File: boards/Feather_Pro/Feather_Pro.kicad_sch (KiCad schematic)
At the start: 45 parts, among them J101 SMA, J102 USB4105-GF-A, J201 TestPoint, SW101 SW_Push, SW102 SW_Push, SW103 SW_SPST, SW104 SW_Push, SW105 SW_Push, U1 LCD_2.2_in, U101 E22-400MM22S, U103 ECMF02-2AMX6, U104 ESP32-S3-MINI-1U, U107 LR2021, U203 TPS2121

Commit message: Connected button to mcu gpio pins
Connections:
- net BUTTON_DOWN: now also U104.8 (IO4)
- net BUTTON_LEFT: now also U104.5 (IO1)
- net BUTTON_RIGHT: now also U104.6 (IO2)
- net BUTTON_UP: now also U104.9 (IO5); no longer C103.2, SW102.2
- net BUTTON_CENTER: now reaches U104.7 (IO3)
- net BUTTON_CENTER: now also C103.2, SW102.2
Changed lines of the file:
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@@
+		)
+	)
+	(hierarchical_label "BUTTON_DOWN"
+		(shape input)
+		(at 229.87 64.77 180)
+		(effects
+			(font
+				(size 1.27 1.27)
+			)
+			(justify right)
 		)
 	)
@@
 		)
 	)
+	(hierarchical_label "BUTTON_CENTER"
+		(shape input)
+		(at 229.87 62.23 180)
+		(effects
+			(font
+				(size 1.27 1.27)
+			)
+			(justify right)
+		)
+	)
 	(hierarchical_label "USB_D+"
 		(shape bidirectional)
@@
 		)
 	)
-	(hierarchical_label "BUTTON_UP"
+	(hierarchical_label "BUTTON_CENTER"
 		(shape input)
 		(at 223.52 135.89 180)
@@
 		)
 	)
+	(hierarchical_label "BUTTON_RIGHT"
+		(shape input)
+		(at 229.87 59.69 180)
+		(effects
+			(font
+				(size 1.27 1.27)
+			)
+			(justify right)
+		)
+	)
 	(hierarchical_label "USB_POWER"
 		(shape output)
@@
 		(effects
 			(font
+				(size 1.27 1.27)
+			)
+			(justify right)
+		)
+	)
+	(hierarchical_label "BUTTON_UP"
+		(shape input)
+		(at 229.87 67.31 180)
+		(effects
+			(font
+				(size 1.27 1.27)
+			)
+			(justify right)
+		)
+	)
+	(hierarchical_label "BUTTON_LEFT"
+		(shape input)
+		(at 229.87 57.15 180)
+		(effects
+			(font

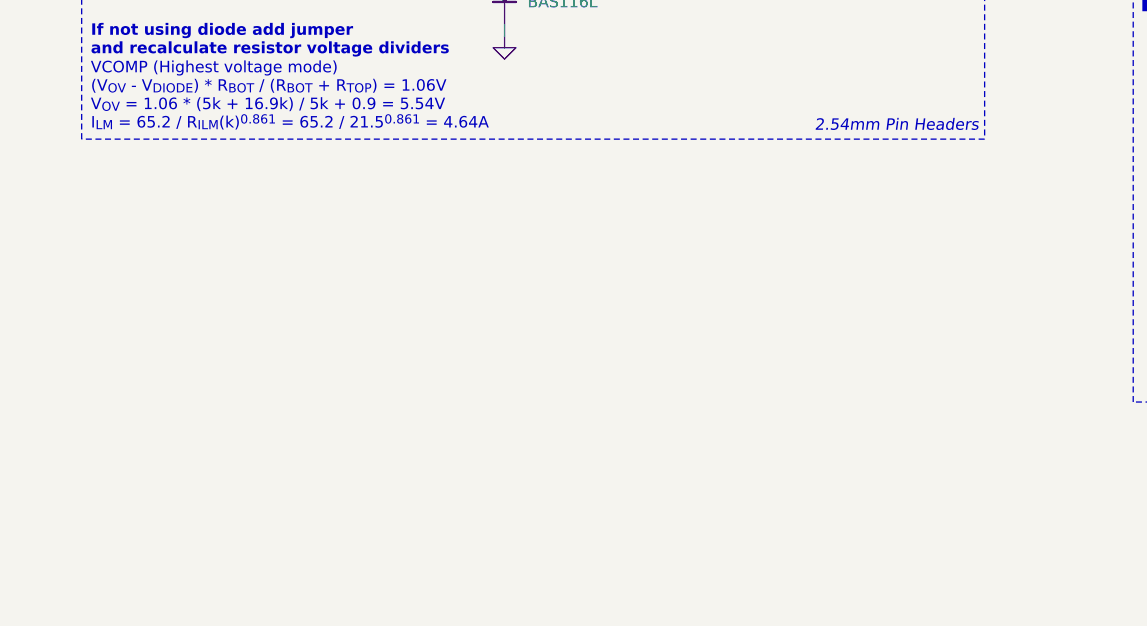
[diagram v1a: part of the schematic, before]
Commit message: Added SD Card Reader
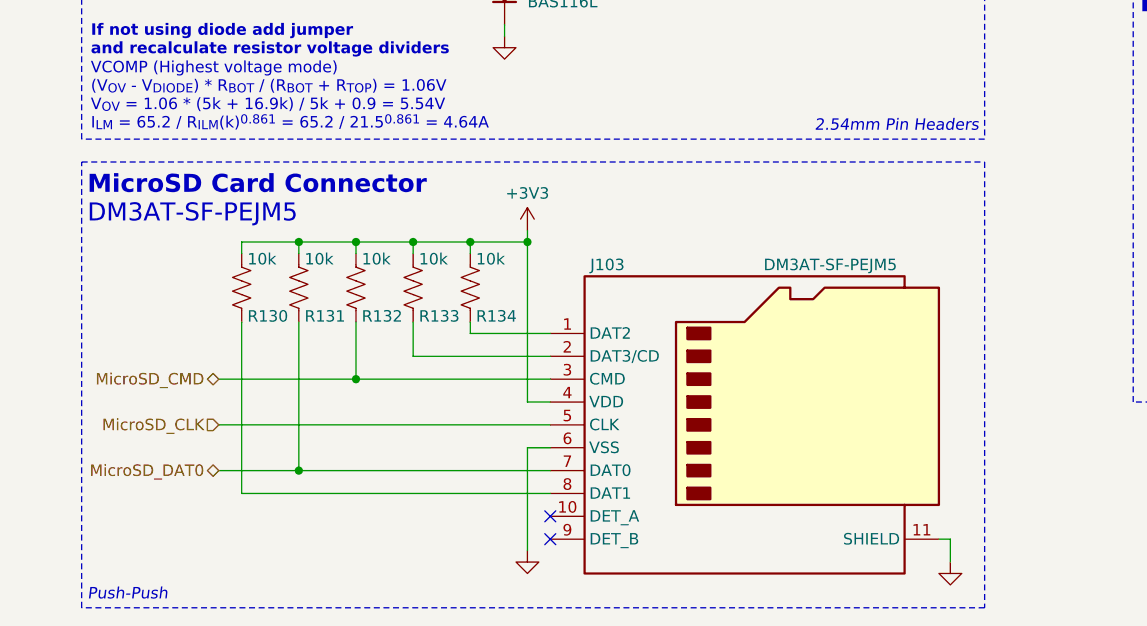
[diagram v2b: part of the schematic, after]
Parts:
- added J103: DM3AT-SF-PEJM5, Connector_Card:microSD_HC_Hirose_DM3AT-SF-PEJM5, symbol Connector:Micro_SD_Card_Det2
- added R130, R131, R132, R133, R134: 10k, Resistor_SMD:R_0603_1608Metric, symbol Device:R_US
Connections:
- net +3V3: now also J103.4 (VDD), R130.2, R131.2, R132.2, R133.2, R134.2
- net GND: now also J103.11 (SHIELD), J103.6 (VSS)
- new net: J103.1 (DAT2), R134.1
- new net: J103.2 (DAT3/CD), R133.1
- new net: J103.8 (DAT1), R130.1
- new net MicroSD_CLK: J103.5 (CLK)
- new net MicroSD_CMD: J103.3 (CMD), R132.1
- new net MicroSD_DAT0: J103.7 (DAT0), R131.1
- no-connect marks 5 -> 7
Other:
- note added: "DM3AT-SF-PEJM5"
- note added: "MicroSD Card Connector"
- note added: "Push-Push"

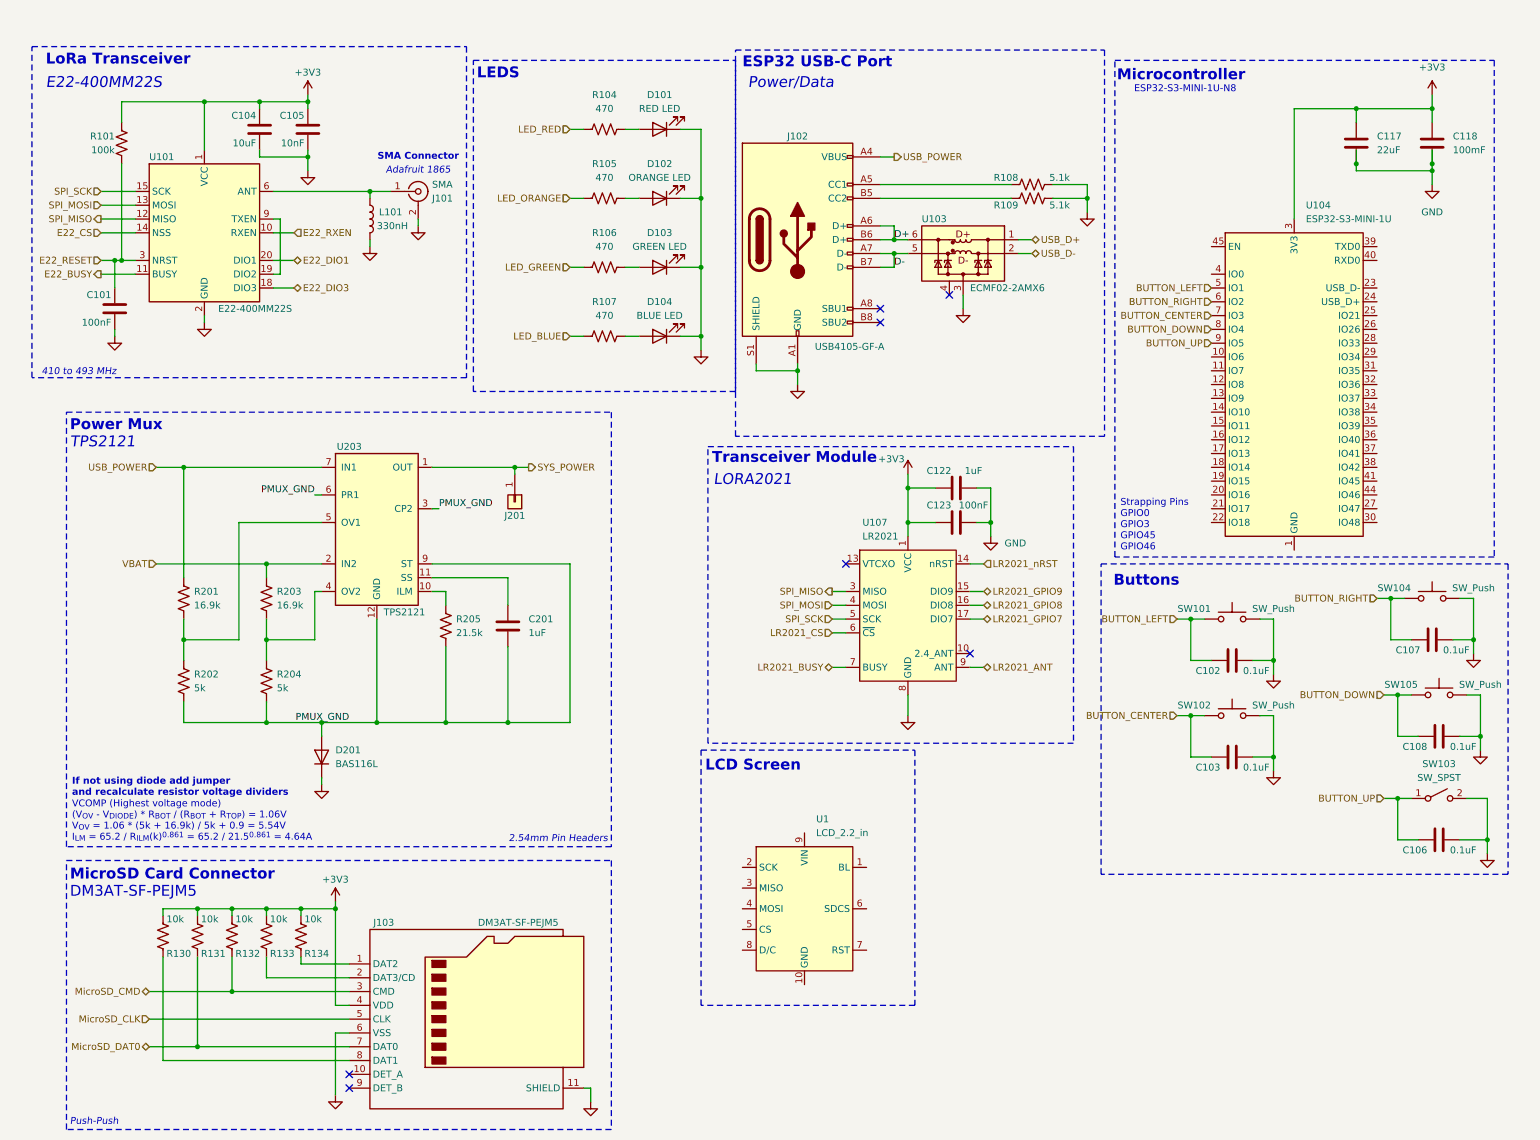
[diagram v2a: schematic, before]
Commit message: Added to schematic and power sheet
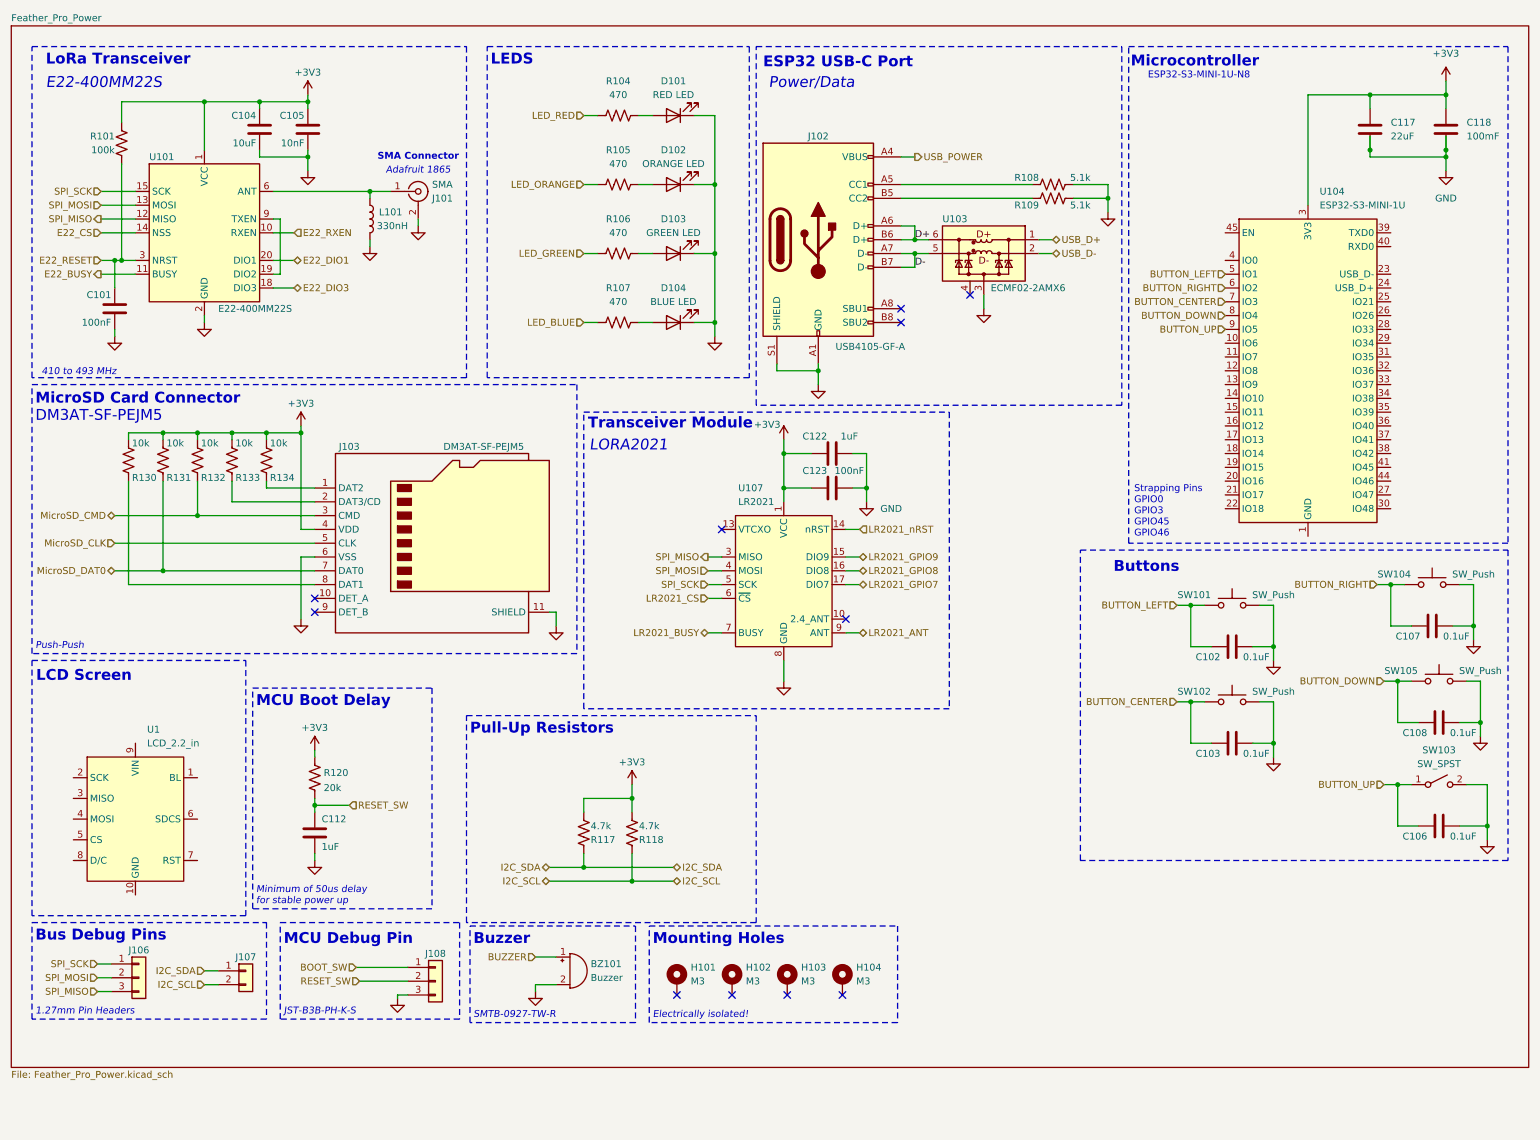
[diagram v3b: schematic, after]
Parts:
- removed C201: 1uF, Capacitor_SMD:C_0402_1005Metric, symbol Device:C
- removed D201: BAS116L, Diode_SMD:D_SOD-882, symbol Device:D
- removed J201: TestPoint, TestPoint:TestPoint_THTPad_1.5x1.5mm_Drill0.7mm, symbol Connector_Generic:Conn_01x01
- removed R201, R203: 16.9k, Resistor_SMD:R_0402_1005Metric, symbol Device:R_US
- removed R202, R204: 5k, Resistor_SMD:R_0402_1005Metric, symbol Device:R_US
- removed R205: 21.5k, Resistor_SMD:R_0402_1005Metric, symbol Device:R_US
- removed U203: TPS2121, Package_DFN_QFN:Texas_VQFN-HR-12_2x2.5mm_P0.5mm, symbol Power_MUX:TPS2121
- added BZ101: Buzzer, Buzzer:Buzzer_SMTB-0927-TW-R, symbol Device:Buzzer
- added C112: 1uF, Capacitor_SMD:C_0402_1005Metric, symbol Device:C
- added H101, H102, H103, H104: M3, MountingHole:MountingHole_3.2mm_M3_Pad_Via, symbol Mechanical:MountingHole_Pad
- added J106: Conn_01x03, Connector_PinHeader_1.27mm:PinHeader_1x03_P1.27mm_Vertical, symbol Connector_Generic:Conn_01x03
- added J107: Conn_01x02, Connector_PinHeader_1.27mm:PinHeader_1x02_P1.27mm_Vertical, symbol Connector_Generic:Conn_01x02
- added J108: Conn_01x03, Connector_JST:JST_PH_B3B-PH-K_1x03_P2.00mm_Vertical, symbol Connector_Generic:Conn_01x03
- added R117, R118: 4.7k, Resistor_SMD:R_0402_1005Metric, symbol Device:R_US
- added R120: 20k, Resistor_SMD:R_0402_1005Metric, symbol Device:R_US
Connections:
- net +3V3: now also R117.2, R118.2, R120.2
- net GND: now also BZ101.2 (-), C112.2, J108.3 (Pin_3)
- net SPI_MISO: now also J106.3 (Pin_3)
- net SPI_MOSI: now also J106.2 (Pin_2)
- net SPI_SCK: now also J106.1 (Pin_1)
- new net BOOT_SW: J108.1 (Pin_1)
- new net BUZZER: BZ101.1 (+)
- new net I2C_SCL: J107.2 (Pin_2), R118.1
- new net I2C_SDA: J107.1 (Pin_1), R117.1
- new net RESET_SW: C112.1, J108.2 (Pin_2), R120.1
- no-connect marks 7 -> 11
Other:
- added sheet Feather_Pro_Power (Feather_Pro_Power.kicad_sch)
- note added: "1.27mm Pin Headers"
- note added: "Bus Debug Pins"
- note added: "Buzzer"
- note added: "Electrically isolated!"
- note added: "JST-B3B-PH-K-S"
- note added: "MCU Boot Delay"
- note added: "MCU Debug Pin"
- note added: "Minimum of 50us delay for stable power up"
- note added: "Mounting Holes"
- note added: "Pull-Up Resistors"
- note added: "SMTB-0927-TW-R"
- note removed: "2.54mm Pin Headers"
- note removed: "If not using diode add jumper and recalculate resistor voltage dividers"
- note removed: "Power Mux"
- note removed: "TPS2121"
- note removed: "VCOMP (Highest voltage mode) (V_{OV} - V_{DIODE}) * R_{BOT} / (R_{BOT} + R_{TOP}) = 1.06V V_{OV} = 1.06 * (5k + 16.9k) / 5k + 0.9 = 5.54V I_{LM} = 65.2 / R_{ILM}(k)^{0.861} = 65.2 / 21.5^{0.861} = 4.64A"
- moved on the sheet: C102, C103, C106, C107, C108, C117, C118, C122, C123, D101, D102, D103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

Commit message: Increased sheet size from A4 to A3 and added contributor information
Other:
- company: (none) -> Illinois Space Society
- title: (none) -> Feather Pro MK1
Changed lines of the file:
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@@
 	(generator "eeschema")
 	(generator_version "10.0")
-	(paper "A4")
+	(paper "A3")
+	(title_block
+		(title "Feather Pro MK1")
+		(rev "A")
+		(company "Illinois Space Society")
+		(comment 3 "Eddie Tang, Bill Wang, Darren Xie")
+		(comment 4 "Arush Borole, Kunal Chattopadhyay, Rohan Das, Agustaya Dhiman, Kacper Paraniuk,")
+	)
 	(rectangle
 		(start 12.7 74.93)
@@
 	(sheet
 		(at 8.89 8.89)
-		(size 279.4 191.77)
+		(size 402.59 279.4)
 		(exclude_from_sim no)
 		(in_bom yes)
@@
 		)
 		(property "Sheetfile" "Feather_Pro_Power.kicad_sch"
-			(at 8.89 201.2446 0)
+			(at 8.89 288.8746 0)
 			(show_name no)
 			(do_not_autoplace no)

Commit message: Added 3V3 Voltage Regulator to schematic
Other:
- sheet Feather_Pro_Power ports: added INA_ALERT, PYRO_SCL, PYRO_SDA, SYS_POWER, USB_POWER, VBAT, VREG_IN; removed none
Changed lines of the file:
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@@
 	)
 	(sheet
-		(at 8.89 8.89)
-		(size 402.59 279.4)
+		(at 201.93 173.99)
+		(size 36.83 25.4)
 		(exclude_from_sim no)
 		(in_bom yes)
@@
 		)
 		(property "Sheetname" "Feather_Pro_Power"
-			(at 8.89 8.1784 0)
+			(at 201.93 173.2784 0)
 			(show_name no)
 			(do_not_autoplace no)
@@
 		)
 		(property "Sheetfile" "Feather_Pro_Power.kicad_sch"
-			(at 8.89 288.8746 0)
+			(at 201.93 199.9746 0)
 			(show_name no)
 			(do_not_autoplace no)
@@
 			)
 		)
+		(pin "INA_ALERT" output
+			(at 201.93 177.8 180)
+			(effects
+				(font
+					(size 1.27 1.27)
+				)
+				(justify left)
+			)
+		)
+		(pin "PYRO_SCL" input
+			(at 201.93 181.61 180)
+			(effects
+				(font
+					(size 1.27 1.27)
+				)
+				(justify left)
+			)
+		)
+		(pin "PYRO_SDA" input
+			(at 201.93 184.15 180)
+			(effects
+				(font
+					(size 1.27 1.27)
+				)
+				(justify left)
+			)
+		)
+		(pin "SYS_POWER" input
+			(at 201.93 186.69 180)
+			(effects
+				(font
+					(size 1.27 1.27)
+				)
+				(justify left)
+			)
+		)
+		(pin "USB_POWER" input
+			(at 201.93 189.23 180)
+			(effects
+				(font
+					(size 1.27 1.27)
+				)
+				(justify left)
+			)
+		)
+		(pin "VBAT" input
+			(at 201.93 191.77 180)
+			(effects
+				(font
+					(size 1.27 1.27)
+				)
+				(justify left)
+			)
+		)
+		(pin "VREG_IN" input
+			(at 201.93 194.31 180)
+			(effects
+				(font
+					(size 1.27 1.27)
+				)
+				(justify left)
+			)
+		)

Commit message: Updated Schematic
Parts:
- added C124: 1uF, Capacitor_SMD:C_0603_1608Metric, symbol Device:C
- added C125: 100nF, Capacitor_SMD:C_0603_1608Metric, symbol Device:C
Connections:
- net +3V3: now also U1.9 (VIN), C124.1, C125.1
- net GND: now also U1.10 (GND), C124.2, C125.2

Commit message: Organized Schematic Sheets
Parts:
- removed C102, C103, C106, C107, C108: 0.1uF, Capacitor_SMD:C_0603_1608Metric, symbol Device:C
- removed C124: 1uF, Capacitor_SMD:C_0603_1608Metric, symbol Device:C
- removed C125: 100nF, Capacitor_SMD:C_0603_1608Metric, symbol Device:C
- removed SW101, SW102, SW104, SW105: SW_Push, Button_Switch_SMD:SW_SPST_FSMSM, symbol Switch:SW_Push
- removed SW103: SW_SPST, Button_Switch_THT:SW_NKK_GW12LJP, symbol Switch:SW_SPST
- removed U1: LCD_2.2_in, symbol LCD_Screen:LCD_2.2_in
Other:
- added sheet Feather_Pro_User_Interface (Feather_Pro_User_Interface.kicad_sch)
- note added: "Power"
- note added: "User Interface Electronics"
- note added: "great work y'all!"
- note removed: "Buttons"
- note removed: "LCD Screen"
- moved on the sheet: BZ101, C101, C104, C105, C112, C117, C118, C122, C123, D101, D102, D103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

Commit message: Started connecting up all the hierarchical labels
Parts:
- added C126: 100pF, Capacitor_SMD:C_0603_1608Metric, symbol Device:C
- added J104: SMA, Connector_Coaxial:SMA_Molex_73251-2120_EdgeMount_Horizontal, symbol Connector:Conn_Coaxial
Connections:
- net BUTTON_CENTER: no longer U104.7 (IO3)
- net BUTTON_DOWN: no longer U104.8 (IO4)
- net BUTTON_LEFT: no longer U104.5 (IO1)
- net BUTTON_RIGHT: no longer U104.6 (IO2)
- net BUTTON_UP: no longer U104.9 (IO5)
- net GND: now also J104.2 (Ext)
- net LR2021_ANT: now also C126.2
- net SPI_MISO: now also U104.13 (IO9)
- net SPI_MOSI: now also U104.11 (IO7)
- net SDA: now reaches U104.10 (IO6)
- net SPI_CLK: now reaches U104.12 (IO8)
- new net: C126.1, J104.1 (In)
- new net SCL: U104.9 (IO5)
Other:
- sheet Feather_Pro_Power ports: added I2C_SCL, I2C_SDA; removed PYRO_SCL, PYRO_SDA
- sheet Feather_Pro_User_Interface ports: added LCD_BL, LCD_CS, LCD_D_C, LCD_RST, LCD_SDCS, SPI_MISO, SPI_MOSI, SPI_SCK; removed none
- moved on the sheet: C101, C104, C105, J101, L101, R101, U101
